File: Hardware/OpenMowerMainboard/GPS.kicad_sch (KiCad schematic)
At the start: 5 parts, among them J47 Conn_01x06_Female, J48 Conn_01x08_Female, J49 Conn_01x08_Female, J50 Conn_01x10_Female

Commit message: BOM changes
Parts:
- XA1: DNP (none) -> Y
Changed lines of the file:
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@@
+      (effects (font (size 1.27 1.27)) hide)
+    )
+    (property "DNP" "Y" (id 5) (at 154.94 77.47 0)
       (effects (font (size 1.27 1.27)) hide)
     )

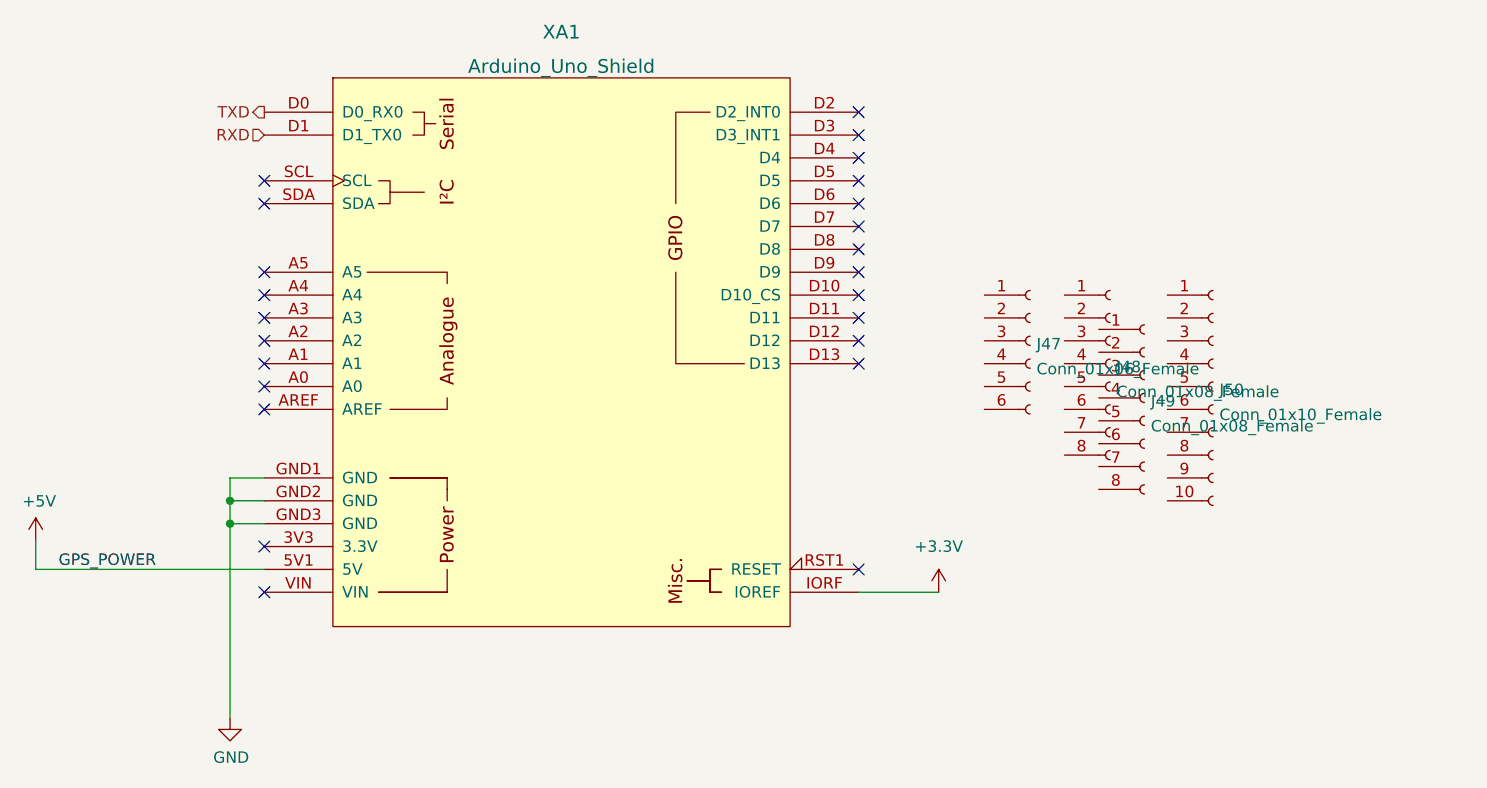
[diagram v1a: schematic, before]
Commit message: fix: fixed ERC/DRC errors, removed LM2596S
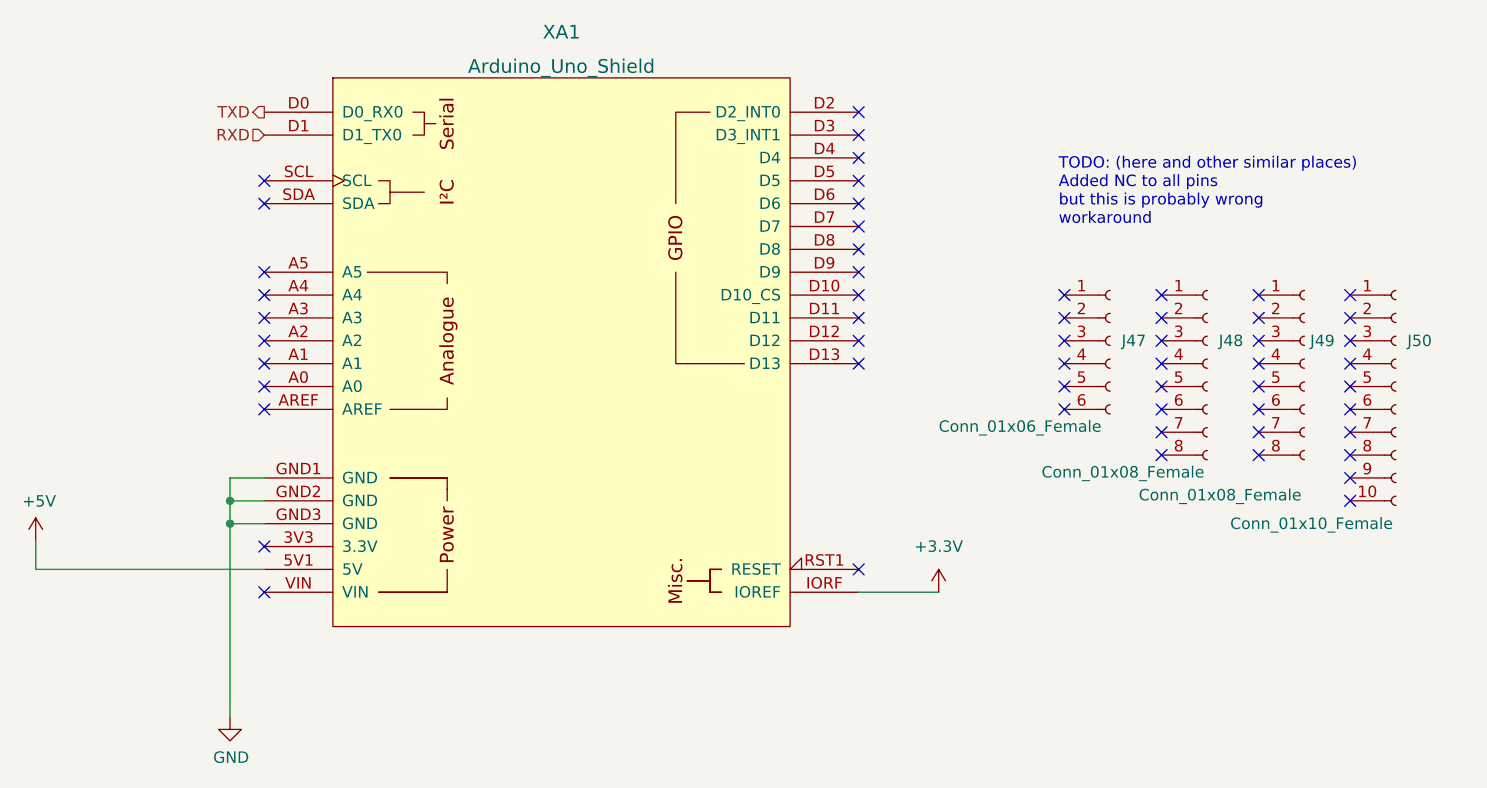
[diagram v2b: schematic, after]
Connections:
- no-connect marks 24 -> 56
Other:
- note added: "TODO: (here and other similar places) Added NC to all pins but this is probably wrong workaround"
- moved on the sheet: J47, J48, J49, J50
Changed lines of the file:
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@@
   (no_connect (at 187.96 60.96))
   (no_connect (at 187.96 101.6))
+  (no_connect (at 210.82 83.82))
+  (no_connect (at 210.82 71.12))
+  (no_connect (at 210.82 73.66))
+  (no_connect (at 210.82 76.2))
+  (no_connect (at 210.82 78.74))
+  (no_connect (at 210.82 81.28))
+  (no_connect (at 221.615 78.74))
+  (no_connect (at 221.615 81.28))
+  (no_connect (at 221.615 83.82))
+  (no_connect (at 221.615 86.36))
+  (no_connect (at 221.615 88.9))
+  (no_connect (at 232.41 88.9))
+  (no_connect (at 232.41 86.36))
+  (no_connect (at 232.41 83.82))
+  (no_connect (at 232.41 81.28))
+  (no_connect (at 242.57 91.44))
+  (no_connect (at 242.57 93.98))
+  (no_connect (at 221.615 71.12))
+  (no_connect (at 221.615 73.66))
+  (no_connect (at 232.41 71.12))
+  (no_connect (at 221.615 76.2))
+  (no_connect (at 232.41 78.74))
+  (no_connect (at 232.41 76.2))
+  (no_connect (at 232.41 73.66))
+  (no_connect (at 242.57 71.12))
+  (no_connect (at 242.57 73.66))
+  (no_connect (at 242.57 76.2))
+  (no_connect (at 242.57 78.74))
+  (no_connect (at 242.57 81.28))
+  (no_connect (at 242.57 83.82))
+  (no_connect (at 242.57 86.36))
+  (no_connect (at 242.57 88.9))
   (no_connect (at 121.92 99.06))
   (no_connect (at 121.92 104.14))
@@
     (stroke (width 0) (type default) (color 0 0 0 0))
   )
-  (label "GPS_POWER" (at 99.06 101.6 0)
+  (text "TODO: (here and other similar places)\nAdded NC to all pins \nbut this is probably wrong\nworkaround"
+    (at 210.185 63.5 0)
     (effects (font (size 1.27 1.27)) (justify left bottom))
   )
@@
     (pin "1")
   )
-  (symbol (lib_id "Connector:Conn_01x10_Female") (at 227.33 81.28 0) (unit 1)
-    (in_bom yes) (on_board no) (fields_autoplaced)
-    (property "Reference" "J50" (id 0) (at 228.0412 81.6415 0)
-      (effects (font (size 1.27 1.27)) (justify left))
-    )
-    (property "Value" "Conn_01x10_Female" (id 1) (at 228.0412 84.4166 0)
-      (effects (font (size 1.27 1.27)) (justify left))
-    )
-    (property "Footprint" "" (id 2) (at 227.33 81.28 0)
-      (effects (font (size 1.27 1.27)) hide)
-    )
-    (property "Datasheet" "~" (id 3) (at 227.33 81.28 0)
-      (effects (font (size 1.27 1.27)) hide)
-    )
-    (property "LCSC" "C35445" (id 4) (at 227.33 81.28 0)
-      (effects (font (size 1.27 1.27)) hide)
-    )
-    (property "Part Number" "C35445" (id 5) (at 227.33 81.28 0)
-      (effects (font (size 1.27 1.27)) hide)
-    )
-    (property "Stock_PN" "J-TH-1x10-.1F" (id 6) (at 227.33 81.28 0)
+  (symbol (lib_id "Connector:Conn_01x10_Female") (at 247.65 81.28 0) (unit 1)
+    (in_bom yes) (on_board no)
+    (property "Reference" "J50" (id 0) (at 248.92 76.2 0)
+      (effects (font (size 1.27 1.27)) (justify left))
+    )
+    (property "Value" "Conn_01x10_Female" (id 1) (at 229.235 96.52 0)
+      (effects (font (size 1.27 1.27)) (justify left))
+    )
+    (property "Footprint" "" (id 2) (at 247.65 81.28 0)
+      (effects (font (size 1.27 1.27)) hide)
+    )
+    (property "Datasheet" "~" (id 3) (at 247.65 81.28 0)
+      (effects (font (size 1.27 1.27)) hide)
+    )
+    (property "LCSC" "C35445" (id 4) (at 247.65 81.28 0)
+      (effects (font (size 1.27 1.27)) hide)
+    )
+    (property "Part Number" "C35445" (id 5) (at 247.65 81.28 0)
+      (effects (font (size 1.27 1.27)) hide)
+    )
+    (property "Stock_PN" "J-TH-1x10-.1F" (id 6) (at 247.65 81.28 0)
       (effects (font (size 1.27 1.27)) hide)
     )
@@
     (pin "1")
   )
-  (symbol (lib_id "Connector:Conn_01x08_Female") (at 219.71 82.55 0) (unit 1)
-    (in_bom yes) (on_board no) (fields_autoplaced)
-    (property "Reference" "J49" (id 0) (at 220.4212 82.9115 0)
-      (effects (font (size 1.27 1.27)) (justify left))
-    )
-    (property "Value" "Conn_01x08_Female" (id 1) (at 220.4212 85.6866 0)
-      (effects (font (size 1.27 1.27)) (justify left))
-    )
-    (property "Footprint" "" (id 2) (at 219.71 82.55 0)
-      (effects (font (size 1.27 1.27)) hide)
-    )
-    (property "Datasheet" "~" (id 3) (at 219.71 82.55 0)
-      (effects (font (size 1.27 1.27)) hide)
-    )
-    (property "LCSC" "C27438" (id 4) (at 219.71 82.55 0)
-      (effects (font (size 1.27 1.27)) hide)
-    )
-    (property "Part Number" "C27438" (id 5) (at 219.71 82.55 0)
-      (effects (font (size 1.27 1.27)) hide)
-    )
-    (property "Stock_PN" "J-TH-1x8-.1F" (id 6) (at 219.71 82.55 0)
+  (symbol (lib_id "Connector:Conn_01x08_Female") (at 237.49 78.74 0) (unit 1)
+    (in_bom yes) (on_board no)
+    (property "Reference" "J49" (id 0) (at 238.125 76.2 0)
+      (effects (font (size 1.27 1.27)) (justify left))
+    )
+    (property "Value" "Conn_01x08_Female" (id 1) (at 219.075 93.345 0)
+      (effects (font (size 1.27 1.27)) (justify left))
+    )
+    (property "Footprint" "" (id 2) (at 237.49 78.74 0)
+      (effects (font (size 1.27 1.27)) hide)
+    )
+    (property "Datasheet" "~" (id 3) (at 237.49 78.74 0)
+      (effects (font (size 1.27 1.27)) hide)
+    )
+    (property "LCSC" "C27438" (id 4) (at 237.49 78.74 0)
+      (effects (font (size 1.27 1.27)) hide)
+    )
+    (property "Part Number" "C27438" (id 5) (at 237.49 78.74 0)
+      (effects (font (size 1.27 1.27)) hide)
+    )
+    (property "Stock_PN" "J-TH-1x8-.1F" (id 6) (at 237.49 78.74 0)
       (effects (font (size 1.27 1.27)) hide)
     )
@@
     (pin "8")
   )
-  (symbol (lib_id "Connector:Conn_01x06_Female") (at 207.01 76.2 0) (unit 1)
-    (in_bom yes) (on_board no) (fields_autoplaced)
-    (property "Reference" "J47" (id 0) (at 207.7212 76.5615 0)
-      (effects (font (size 1.27 1.27)) (justify left))
-    )
-    (property "Value" "Conn_01x06_Female" (id 1) (at 207.7212 79.3366 0)
-      (effects (font (size 1.27 1.27)) (justify left))
-    )
-    (property "Footprint" "" (id 2) (at 207.01 76.2 0)
-      (effects (font (size 1.27 1.27)) hide)
-    )
-    (property "Datasheet" "~" (id 3) (at 207.01 76.2 0)
-      (effects (font (size 1.27 1.27)) hide)
-    )
-    (property "LCSC" "C40877" (id 4) (at 207.01 76.2 0)
-      (effects (font (size 1.27 1.27)) hide)
-    )
-    (property "Part Number" "C40877" (id 5) (at 207.01 76.2 0)
-      (effects (font (size 1.27 1.27)) hide)
-    )
-    (property "Stock_PN" "J-TH-1x6-.1F" (id 6) (at 207.01 76.2 0)
+  (symbol (lib_id "Connector:Conn_01x06_Female") (at 215.9 76.2 0) (unit 1)
+    (in_bom yes) (on_board no)
+    (property "Reference" "J47" (id 0) (at 217.17 76.2 0)
+      (effects (font (size 1.27 1.27)) (justify left))
+    )
+    (property "Value" "Conn_01x06_Female" (id 1) (at 196.85 85.725 0)
+      (effects (font (size 1.27 1.27)) (justify left))
+    )
+    (property "Footprint" "" (id 2) (at 215.9 76.2 0)
+      (effects (font (size 1.27 1.27)) hide)
+    )
+    (property "Datasheet" "~" (id 3) (at 215.9 76.2 0)
+      (effects (font (size 1.27 1.27)) hide)
+    )
+    (property "LCSC" "C40877" (id 4) (at 215.9 76.2 0)
+      (effects (font (size 1.27 1.27)) hide)
+    )
+    (property "Part Number" "C40877" (id 5) (at 215.9 76.2 0)
+      (effects (font (size 1.27 1.27)) hide)
+    )
+    (property "Stock_PN" "J-TH-1x6-.1F" (id 6) (at 215.9 76.2 0)
       (effects (font (size 1.27 1.27)) hide)
     )
@@
     (pin "6")
   )
-  (symbol (lib_id "Connector:Conn_01x08_Female") (at 215.9 78.74 0) (unit 1)
-    (in_bom yes) (on_board no) (fields_autoplaced)
-    (property "Reference" "J48" (id 0) (at 216.6112 79.1015 0)
-      (effects (font (size 1.27 1.27)) (justify left))
-    )
-    (property "Value" "Conn_01x08_Female" (id 1) (at 216.6112 81.8766 0)
-      (effects (font (size 1.27 1.27)) (justify left))
-    )
-    (property "Footprint" "" (id 2) (at 215.9 78.74 0)
-      (effects (font (size 1.27 1.27)) hide)
-    )
-    (property "Datasheet" "~" (id 3) (at 215.9 78.74 0)
-      (effects (font (size 1.27 1.27)) hide)
-    )
-    (property "LCSC" "C27438" (id 4) (at 215.9 78.74 0)
-      (effects (font (size 1.27 1.27)) hide)
-    )
-    (property "Part Number" "C27438" (id 5) (at 215.9 78.74 0)
-      (effects (font (size 1.27 1.27)) hide)
-    )
-    (property "Stock_PN" "J-TH-1x8-.1F" (id 6) (at 215.9 78.74 0)
-      (effects (font (size 1.27 1.27)) hide)
-    )
+  (symbol (lib_id "Connector:Conn_01x08_Female") (at 226.695 78.74 0) (unit 1)
+    (in_bom yes) (on_board no)
+    (property "Reference" "J48" (id 0) (at 227.965 76.2 0)
+      (effects (font (size 1.27 1.27)) (justify left))
+    )
+    (property "Value" "Conn_01x08_Female" (id 1) (at 208.28 90.805 0)
+      (effects (font (size 1.27 1.27)) (justify left))
+    )
+    (property "Footprint" "" (id 2) (at 226.695 78.74 0)
+      (effects (font (size 1.27 1.27)) hide)
+    )
+    (property "Datasheet" "~" (id 3) (at 226.695 78.74 0)
+      (effects (font (size 1.27 1.27)) hide)
+    )
+    (property "LCSC" "C27438" (id 4) (at 226.695 78.74 0)
+      (effects (font (size 1.27 1.27)) hide)
+    )
+    (property "Part Number" "C27438" (id 5) (at 226.695 78.74 0)
+      (effects (font (size 1.27 1.27)) hide)
+    )
+    (property "Stock_PN" "J-TH-1x8-.1F" (id 6) (at 226.695 78.74 0)
+      (effects (font (size 1.27 1.27)) hide)
+    )

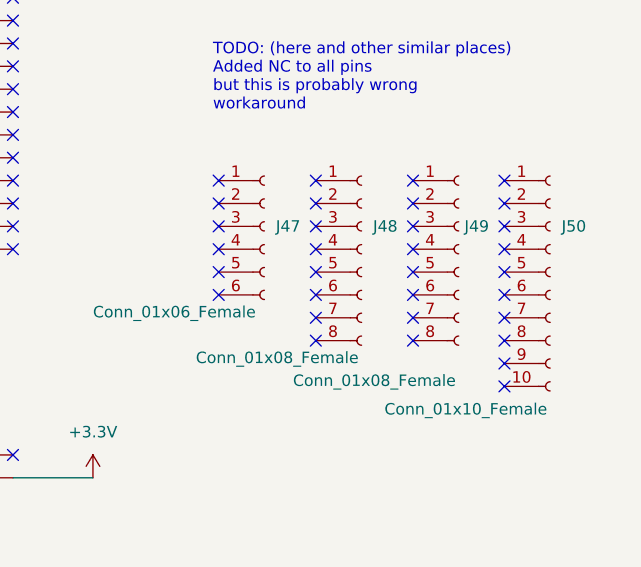
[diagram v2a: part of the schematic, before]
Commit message: feat: update to Kicad7, put back C2,C3
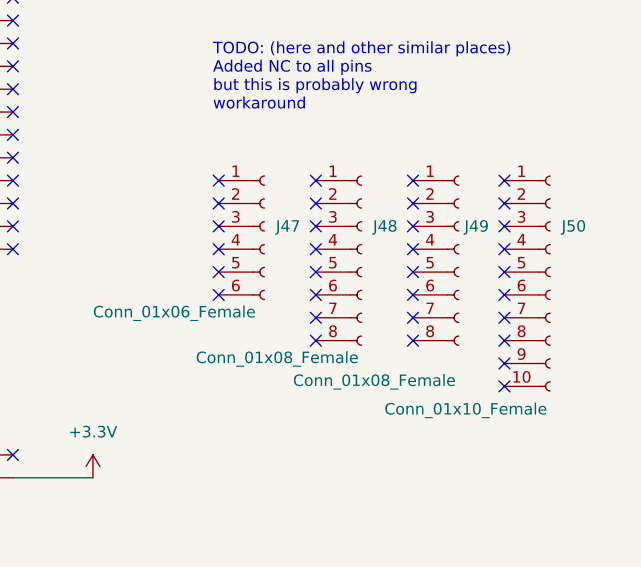
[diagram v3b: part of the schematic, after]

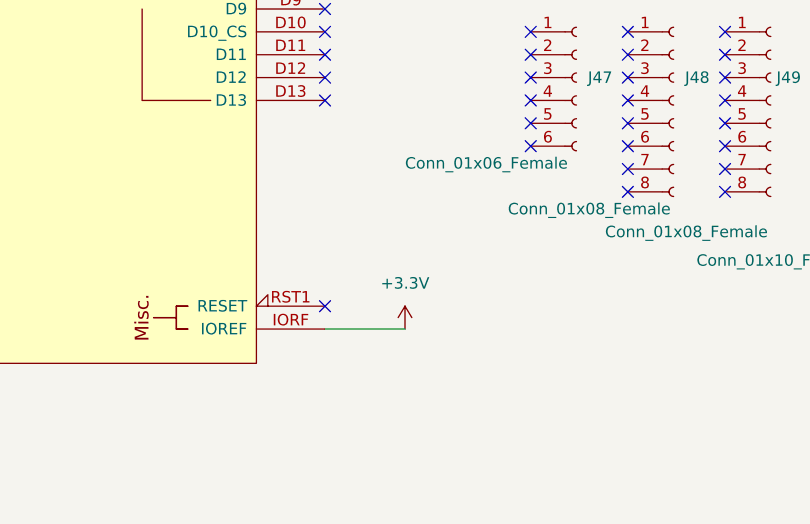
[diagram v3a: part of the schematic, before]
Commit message: upgraded to KiCAD v8
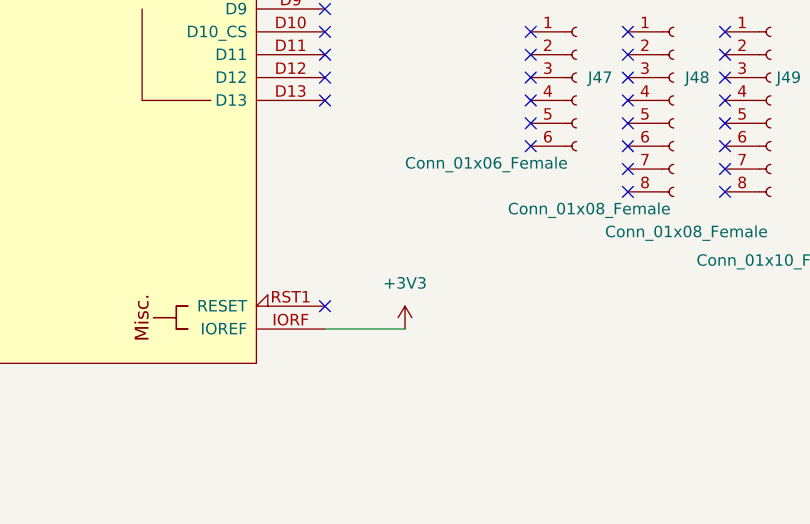
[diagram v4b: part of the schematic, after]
